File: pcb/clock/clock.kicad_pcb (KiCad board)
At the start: 2 copper layers, 100 x 100 mm, 29 parts, among them J1 Conn_02x05_Odd_Even, Q1 Q_PMOS_GSD, Q2 Q_PMOS_GSD, Q3 Q_PMOS_GSD, Q4 HX2301A, SW1 SW_DIP_x01, SW2 SW_DIP_x01, U1 LSD080BAG-103A-01, U2 LSD080BAG-103A-01, U3 74HC595, U4 LSD080BAG-103A-01, U5 LSD080BAG-103A-01, U6 74HC595

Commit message: first complete pcb of the clock
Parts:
- C4, C5, R1, R2, R3, R4: moved to B.Cu
- moved U3 158.8 mm to (171.5, 101.5), turned to -90 degrees
- moved U6 134.1 mm to (156.9, 101.4), turned to -90 degrees
- moved Q4 129.0 mm to (178.0, 94.7), turned to -90 degrees
- moved R4 126.4 mm to (175.2, 94.9), turned to 90 degrees
- moved C5 121.5 mm to (179.2, 101.5), turned to 90 degrees
- moved C4 121.4 mm to (149.0, 101.7), turned to 90 degrees
- moved Q2 120.9 mm to (122.9, 92.2), turned to -90 degrees
- moved R9 116.0 mm to (144.8, 108.6), turned to -90 degrees
- moved Q3 115.6 mm to (148.2, 94.6), turned to -90 degrees
- moved R5 112.3 mm to (159.4, 131.0), turned to 180 degrees
- moved R6 107.3 mm to (159.4, 133.8)
- moved R3 104.3 mm to (145.1, 94.3), turned to 90 degrees
- moved C1 100.5 mm to (159.4, 136.6), turned to 180 degrees
- moved D1 96.3 mm to (144.8, 112.9), turned to 90 degrees
- moved R7 83.9 mm to (130.3, 131.0)
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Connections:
- U3 pad 3: E -> D
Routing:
- net VCC: track 0.00 -> 211.4 mm, vias 0 -> 13
- net A: track 0.00 -> 191.8 mm, vias 0 -> 5
- net B: track 0.00 -> 184.7 mm, vias 0 -> 4
- net F: track 0.00 -> 181.1 mm, vias 0 -> 4
- net GND: track 0.00 -> 178.3 mm, vias 0 -> 2
- net C: track 0.00 -> 174.4 mm, vias 0 -> 5
- net G: track 0.00 -> 171.6 mm
- net E: track 0.00 -> 154.8 mm, vias 0 -> 1
- net D: track 0.00 -> 142.2 mm, vias 0 -> 6
- net /m1_pow: track 0.00 -> 110.6 mm, vias 0 -> 1
- net P: track 0.00 -> 108.1 mm, vias 0 -> 6
- net H1: track 0.00 -> 70.6 mm
- net SDATA: track 0.00 -> 59.6 mm, vias 0 -> 2
- net /SW1: track 0.00 -> 58.9 mm, vias 0 -> 1
- net LATCH: track 0.00 -> 55.2 mm, vias 0 -> 2
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- added copper zone on B.Cu, net GND
- added copper zone on F.Cu, net VCC

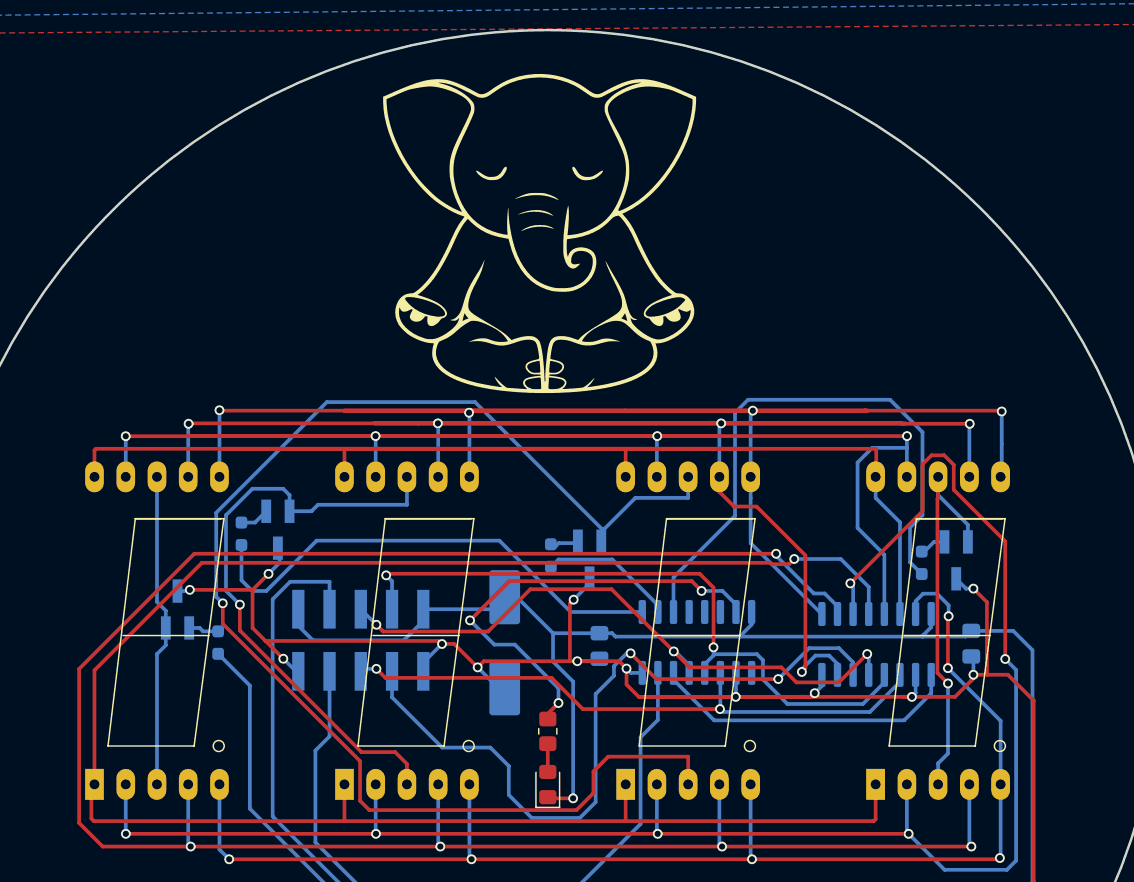
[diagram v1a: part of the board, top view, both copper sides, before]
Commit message: new version. tried to fix the busg in v1
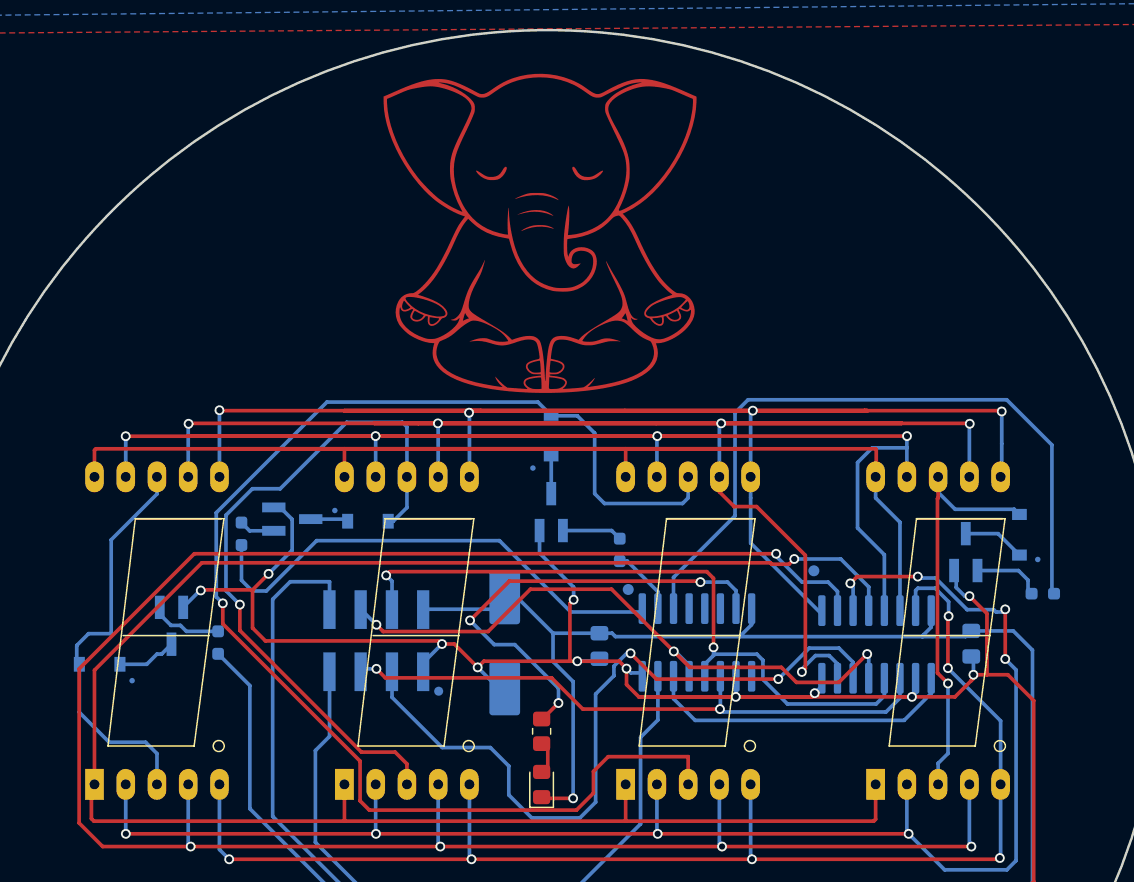
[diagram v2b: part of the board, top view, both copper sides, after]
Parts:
- added D2: RB160M-30, Diode_SMD:D_SOD-123, B.Cu at (108.4, 103.2)
- added D3: RB160M-30, Diode_SMD:D_SOD-123, B.Cu at (130.2, 91.5)
- added D4: RB160M-30, Diode_SMD:D_SOD-123, B.Cu at (145.1, 84.6)
- added D5: RB160M-30, Diode_SMD:D_SOD-123, B.Cu at (183.1, 92.6)
- C4, C5: value 100n -> 10u
- G***: footprint graphics:elephant -> graphics:elephant_copper
- J1: value Conn_02x05_Odd_Even -> Conn_02x04_Odd_Even; footprint Connector_PinHeader_2.54mm:PinHeader_2x05_P2.54mm_Vertical_SMD -> Connector_PinHeader_2.54mm:PinHeader_2x04_P2.54mm_Vertical_SMD
- Q1, Q2, Q3: value Q_PMOS_GSD -> HX2301A
- U3, U6: footprint Package_SO:SOIC-16_3.9x9.9mm_P1.27mm -> components:SOIC-16_3.9x9.9mm_P1.27mm_handsolder
- moved R4 10.2 mm to (185.0, 97.4), turned to 180 degrees
- moved R3 5.62 mm to (150.7, 93.8)
- moved Q3 4.96 mm to (145.1, 90.8), turned to 90 degrees
- moved Q2 1.45 mm to (124.0, 91.3), turned to 0 degrees
- moved Q1 1.41 mm to (114.2, 100.0), turned to -90 degrees
- moved J1 1.26 mm to (130.9, 101.2)
- moved Q4 1.03 mm to (178.8, 94.0), turned to 90 degrees
- moved D1 0.50 mm to (144.3, 112.9)
- moved R9 0.50 mm to (144.3, 108.6)
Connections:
- net A renamed /A
- net B renamed /B
- net C renamed /C
- net D renamed /D
- net E renamed /E
- net F renamed /F
- net G renamed /G
- net P renamed /DP
- C3 pad 1: VCC -> +3V3
- C4 pad 1: VCC -> +3V3
- C5 pad 1: VCC -> +3V3
- J1 pad 1: VCC -> +3V3
- Q1 pad 2: /h1_pow -> +3V3
- Q1 pad 3: VCC -> Net-(Q1-Pad3)
- Q2 pad 2: /h2_pow -> +3V3
- Q2 pad 3: VCC -> Net-(Q2-Pad3)
- Q3 pad 2: /m1_pow -> +3V3
- Q3 pad 3: VCC -> Net-(Q3-Pad3)
- Q4 pad 2: /m2_pow -> +3V3
- Q4 pad 3: VCC -> Net-(Q4-Pad3)
- R5 pad 1: VCC -> +3V3
- R7 pad 1: VCC -> +3V3
- U3 pad 10: VCC -> +3V3
- U3 pad 16: VCC -> +3V3
- U6 pad 10: VCC -> +3V3
- U6 pad 16: VCC -> +3V3
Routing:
- net +3V3: track 0.00 -> 217.6 mm, vias 0 -> 12
- net VCC: track 211.4 -> 0.00 mm, vias 13 -> 0
- net /D: track 142.2 -> 127.5 mm, vias 6 -> 8
- net GND: track 178.3 -> 165.7 mm
- net M2: track 47.4 -> 58.1 mm
- net /h1_pow: track 25.6 -> 33.2 mm
- net /h2_pow: track 49.2 -> 56.1 mm
- net M1: track 11.3 -> 5.78 mm
- net Net-(Q4-Pad3): track 0.00 -> 5.08 mm
- net Net-(Q1-Pad3): track 0.00 -> 4.87 mm
- net Net-(Q4-Pad1): track 2.18 -> 5.65 mm
- net Net-(Q1-Pad1): track 2.46 -> 5.88 mm
- net Net-(Q3-Pad3): track 0.00 -> 3.07 mm
- net Net-(Q2-Pad3): track 0.00 -> 3.07 mm
- net Net-(Q3-Pad1): track 2.53 -> 4.89 mm
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- added copper zone on F.Cu, net +3V3
- removed copper zone on F.Cu, net VCC
